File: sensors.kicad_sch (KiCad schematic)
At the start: 26 parts

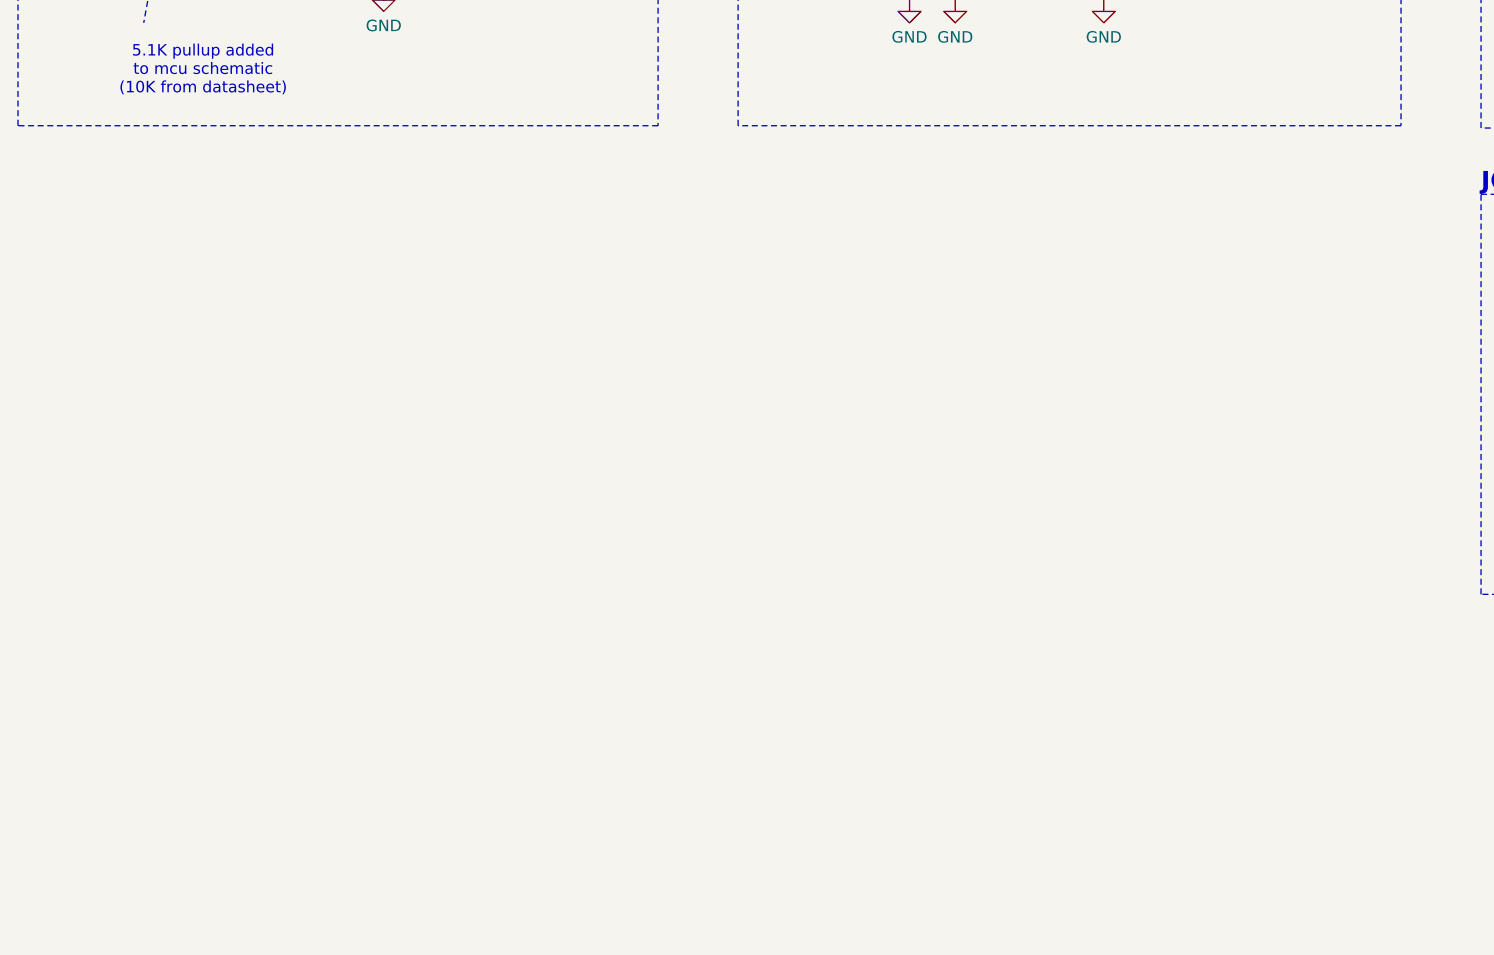
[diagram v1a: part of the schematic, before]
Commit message: Completated the Power Schema + Added Shunts resistors with OP Amp + Connected the RGB Connector to the BUCK (Fixes #5)
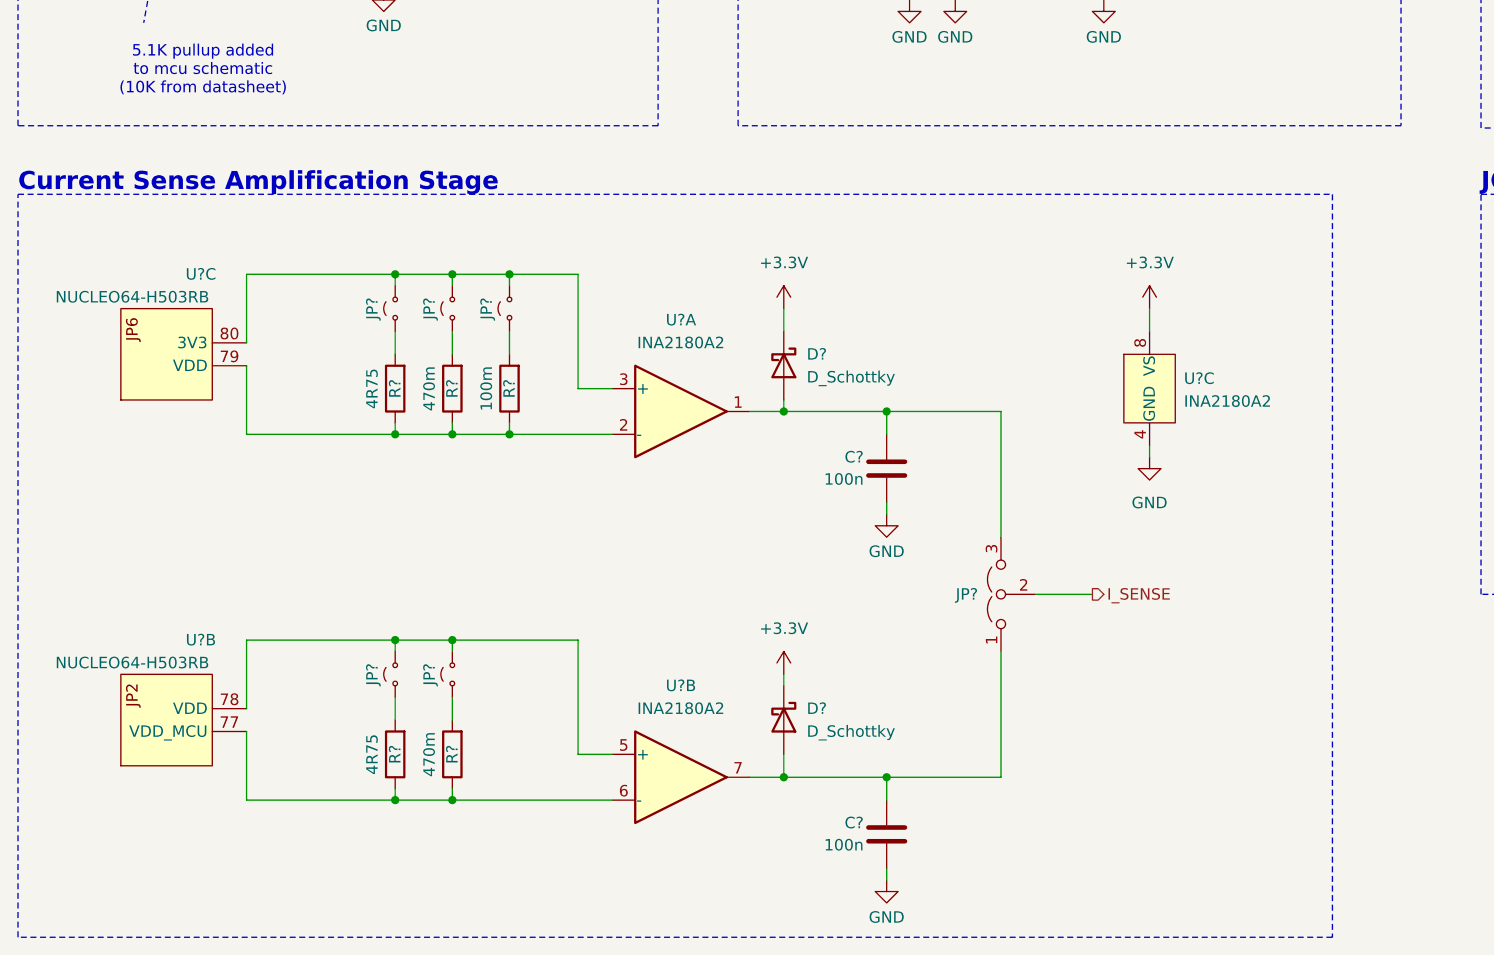
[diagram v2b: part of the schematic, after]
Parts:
- added C? (x2): 100n, Capacitor_SMD:C_0402_1005Metric, symbol Device:C
- added D? (x2): D_Schottky, symbol Device:D_Schottky
- added JP?: Jumper_3_Open, Connector_PinHeader_2.54mm:PinHeader_1x03_P2.54mm_Vertical, symbol Jumper:Jumper_3_Open
- added JP? (x5): Jumper_2_Small_Open, Connector_PinHeader_2.54mm:PinHeader_1x02_P2.54mm_Vertical, symbol Jumper:Jumper_2_Small_Open
- added R? (x2): 470m, symbol Device:R
- added R? (x2): 4R75, symbol Device:R
- added R?: 100m, symbol Device:R
- added U?: INA2180A2, Package_SO:VSSOP-8_3x3mm_P0.65mm, symbol ProjectAmplifiers:INA2180A2_VSSOP-8
- added U? (x2): NUCLEO64-H503RB, ProjectConnectors:Nucleo64, symbol ProjectMCUs:NUCLEO64-H503RB
- added U? (x2): INA2180A2, Package_SO:VSSOP-8_3x3mm_P0.65mm, symbol OP_AMP:INA2180A2_VSSOP-8
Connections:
- net GND: now also C?.2, C?.2, U?.4 (GND)
- new net: C?.1, D?.2 (A), JP?.1 (A), U?.7
- new net: R?.1, R?.1, U?.6 (-), U?.77 (VDD_MCU)
- new net: JP?.1 (A), R?.2 (x5)
- new net: C?.1, D?.2 (A), JP?.3 (B), U?.1
- new net: JP?.2 (B), JP?.2 (B), U?.5 (+), U?.78 (VDD)
- new net: R?.1, R?.1, R?.1, U?.2 (-), U?.79 (VDD)
- new net: JP?.2 (B), JP?.2 (B), JP?.2 (B), U?.3 (+), U?.80 (3V3)
- new net +3.3V: D?.1 (K), D?.1 (K), U?.8 (VS)
- new net I_SENSE: JP?.2 (C)
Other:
- note added: "Current Sense Amplification Stage"

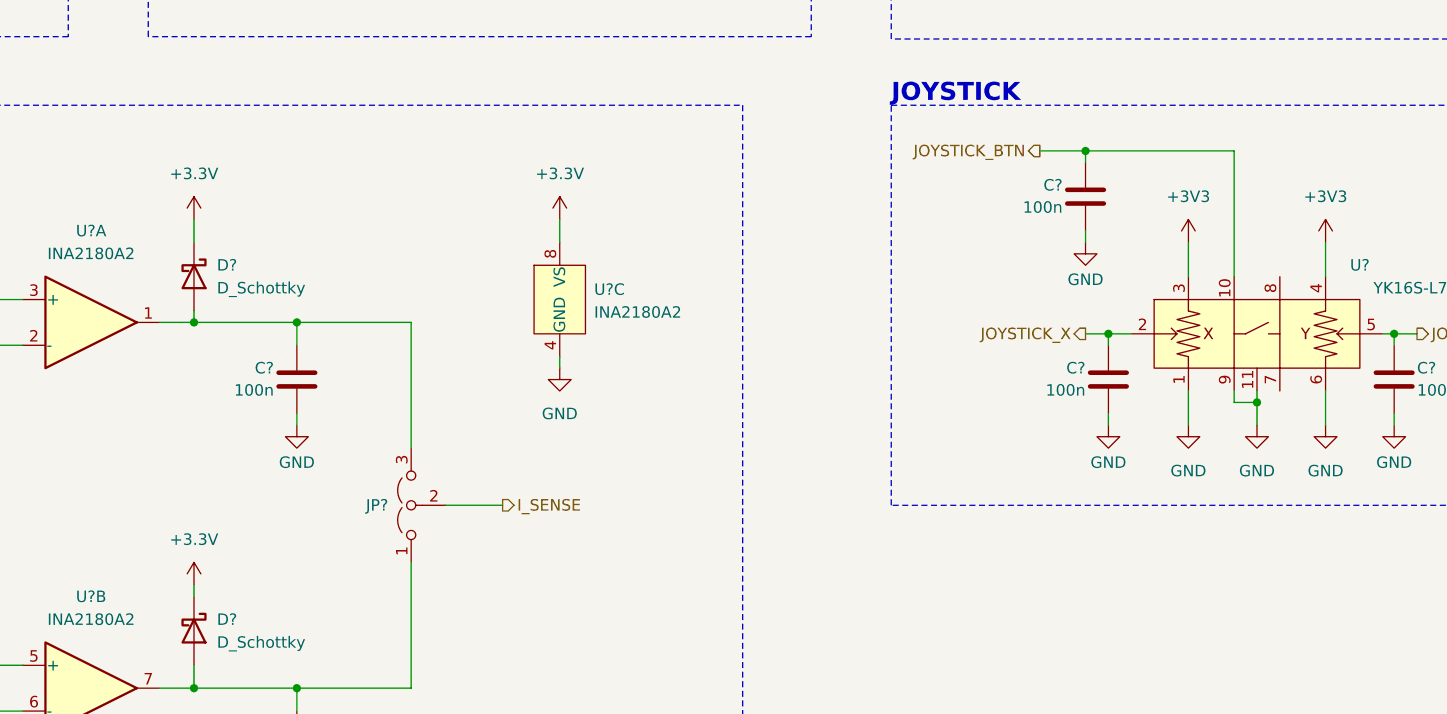
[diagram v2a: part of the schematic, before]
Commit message: Runned ERC for the first time and fixed some errors
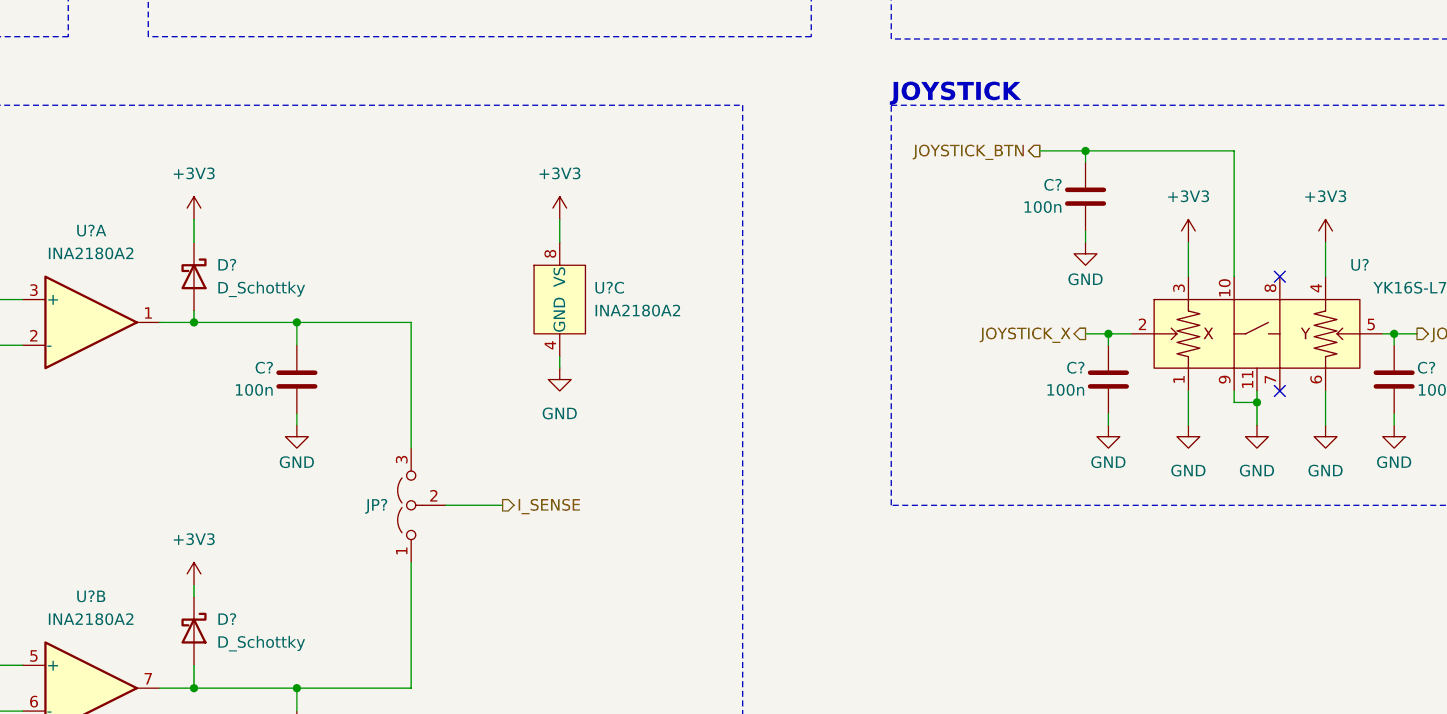
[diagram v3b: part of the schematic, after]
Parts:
- removed U?: INA2180A2, Package_SO:VSSOP-8_3x3mm_P0.65mm, symbol ProjectAmplifiers:INA2180A2_VSSOP-8
- removed U? (x2): INA2180A2, Package_SO:VSSOP-8_3x3mm_P0.65mm, symbol OP_AMP:INA2180A2_VSSOP-8
- added U? (x3): INA2180A2, Package_SO:VSSOP-8_3x3mm_P0.65mm, symbol ProjectAmplifiers:INA2180A2_VSSOP-8
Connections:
- net +3.3V is gone; now on net +3V3: D?.1 (K), D?.1 (K)
- net +3V3: now also U?.8 (VS)
- net GND: now also U?.4 (GND)
- net at C?.1, D?.2 (A), JP?.1 (A): now also U?.7
- net at R?.1, R?.1, U?.77 (VDD_MCU): now also U?.6 (-)
- net at C?.1, D?.2 (A), JP?.3 (B): now also U?.1
- net at JP?.2 (B), JP?.2 (B), U?.78 (VDD): now also U?.5 (+)
- net at R?.1, R?.1, R?.1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: now also U?.2 (-)
- net at JP?.2 (B), JP?.2 (B), JP?.2 (B)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: now also U?.3 (+)
- no-connect marks 1 -> 3

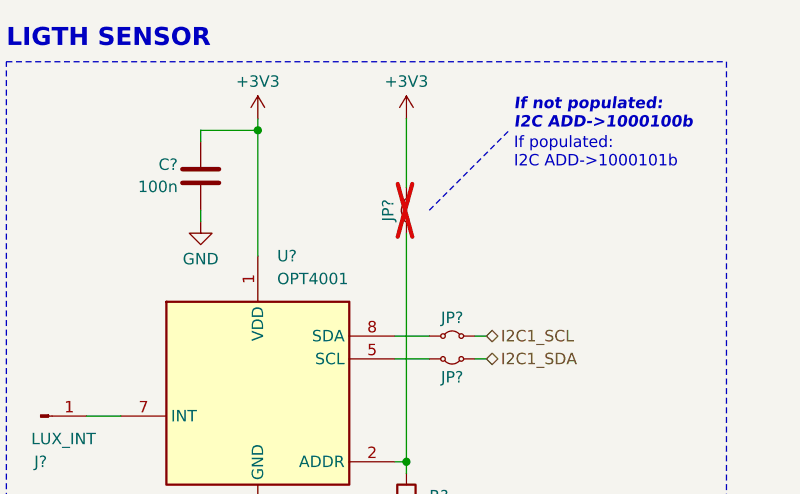
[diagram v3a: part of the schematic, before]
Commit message: Changed some value for grouping components
Basically two resistors valued 5.1k and 5K1 have the same value
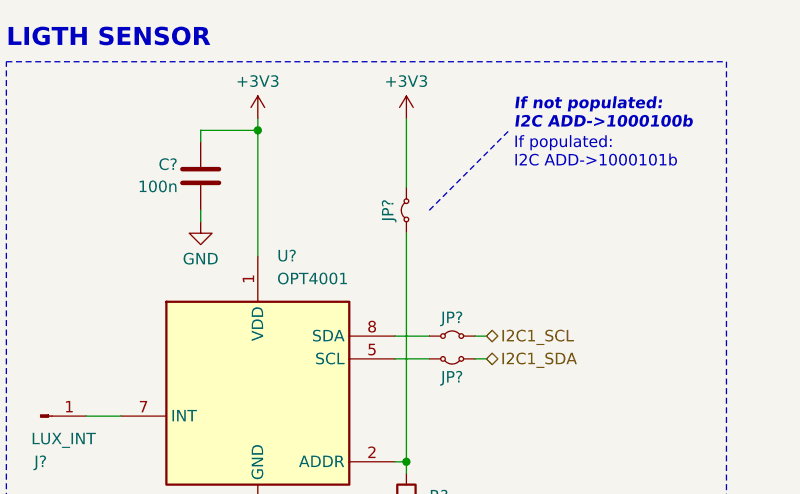
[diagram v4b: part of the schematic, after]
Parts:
- JP?: now fitted
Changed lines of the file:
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@@
 		(in_bom yes)
 		(on_board yes)
-		(dnp yes)
+		(dnp no)
 		(property "Reference" "JP?"
 			(at 229.108 39.37 0)
